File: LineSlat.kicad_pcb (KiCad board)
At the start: 4 copper layers, 100 x 160 mm, 130 parts, among them J4 DEBUG, J5 RJ45, J6 RJ45, J7 USB_B_Micro, J8 BATT, Q1 DMG3402, Q10 MMBT3904L, Q12 DMN6075S, Q13 MMBT3906, Q2 DMG3402, Q3 DMG3402, Q4 DMG3402, Q5 DMG3402, Q6 DMG3402, Q7 DMP3099L, Q8 MMBT3904L, Q9 DMN6075S, SW1 SPDT, SW2 SPDT, SW3 RESET, U1 THVD1400D, U2 THVD1400D, U3 RFM95W-915S2, U4 ATSAMD21G18A-A, U5 TSR1-2433E, Y1 32.768K-12.5p

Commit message: Change diodes and regulator
Changed regulator from TSR-1-2433E to TSR-1-2433
This changes Vin minimum from 6V to 4.76V

Changed schottky diodes to BAT54W.
This fixes 2 issues:
- reverse voltage 20V -> 30V (not enough margin for ~20V LiPo)
- forward voltage drop 600mV -> 250mV (5V-600mV is below Vin min of 3.3V regulator)
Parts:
- D3, D4: value SD103CW -> BAT54W
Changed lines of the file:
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@@
 			)
 		)
-		(property "Value" "SD103CW"
+		(property "Value" "BAT54W"
 			(at 0 2.1 90)
 			(layer "F.Fab")
@@
 			)
 		)
-		(property "Mouser Part Number" "78-SD103CW-HE3_A-08 "
+		(property "Mouser Part Number" "78-BAT54W-HG3-18 "
 			(at 0 0 90)
 			(unlocked yes)
@@
 			)
 		)
-		(property "Value" "SD103CW"
+		(property "Value" "BAT54W"
 			(at 0 2.1 90)
 			(layer "F.Fab")
@@
 			)
 		)
-		(property "Mouser Part Number" "78-SD103CW-HE3_A-08 "
+		(property "Mouser Part Number" "78-BAT54W-HG3-18 "
 			(at 0 0 -90)
 			(unlocked yes)

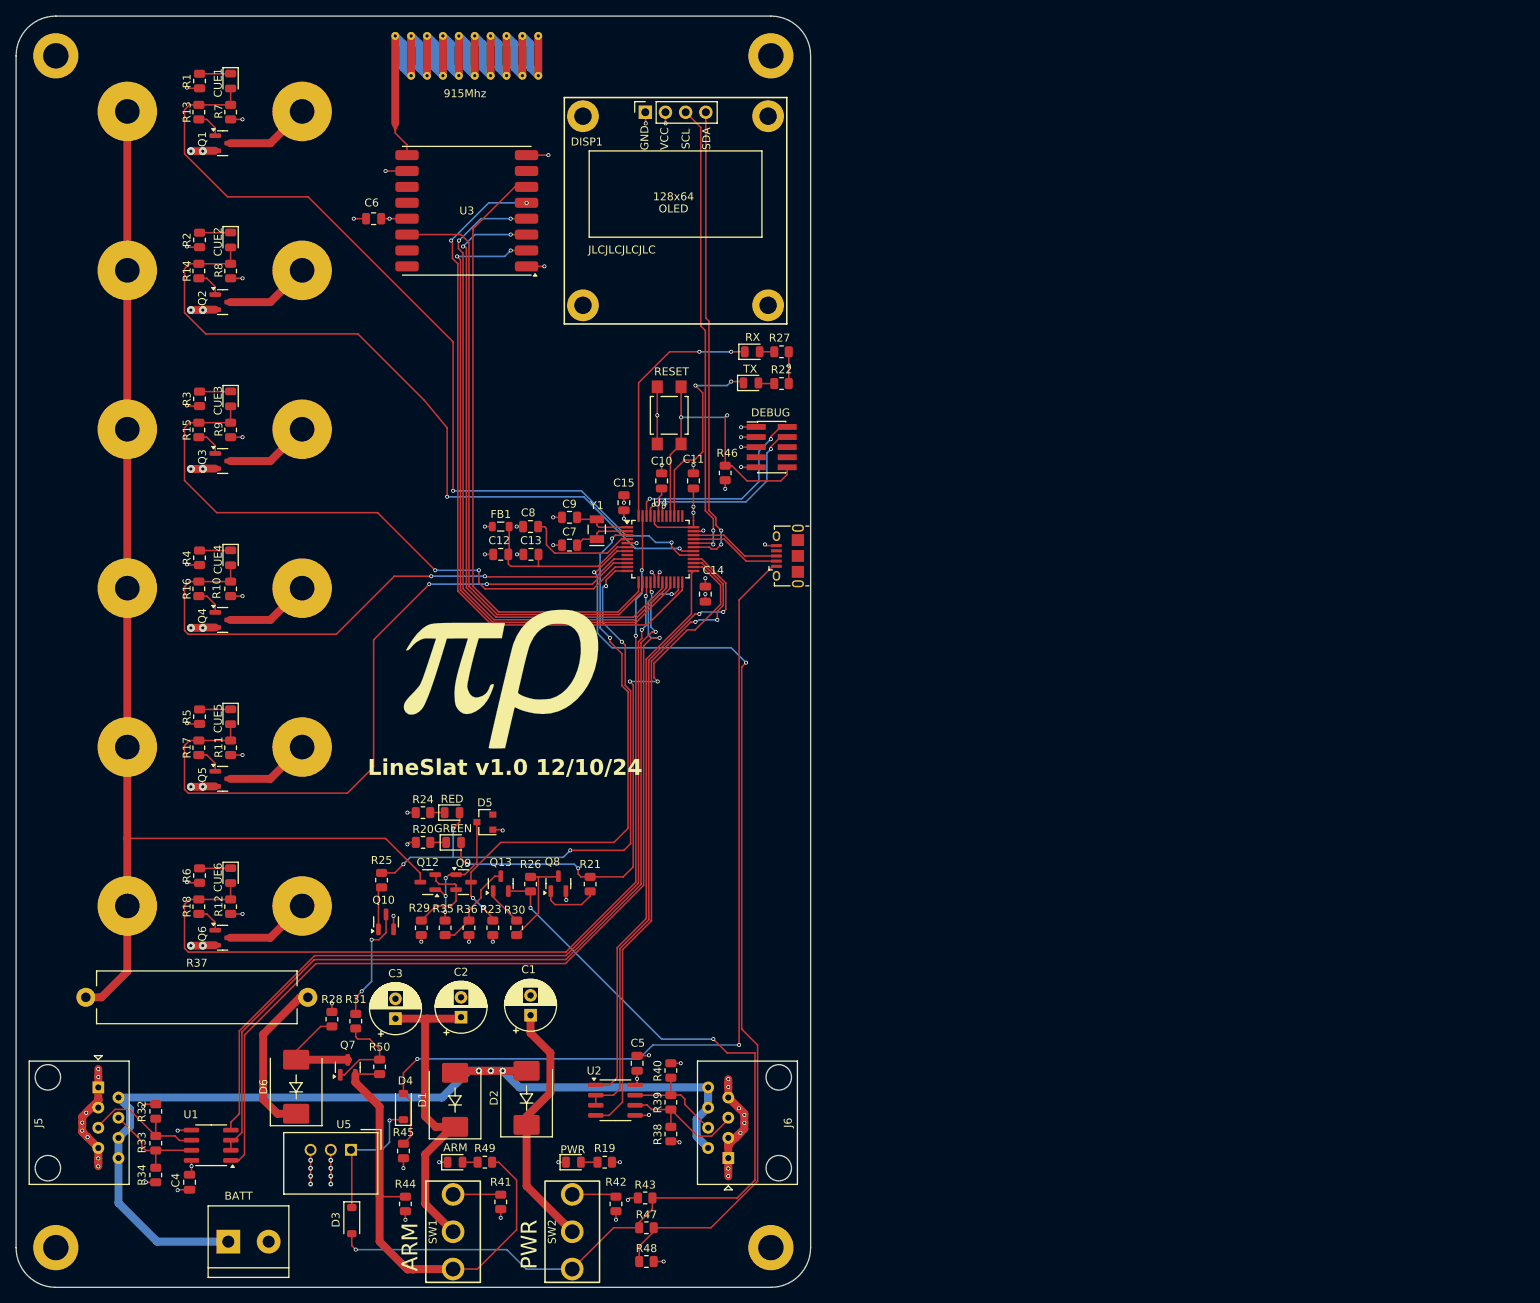
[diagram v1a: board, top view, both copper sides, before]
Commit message: v2.0
* new continuity test using INA219
* 8 cues instead of 6
* Lots of minor changes
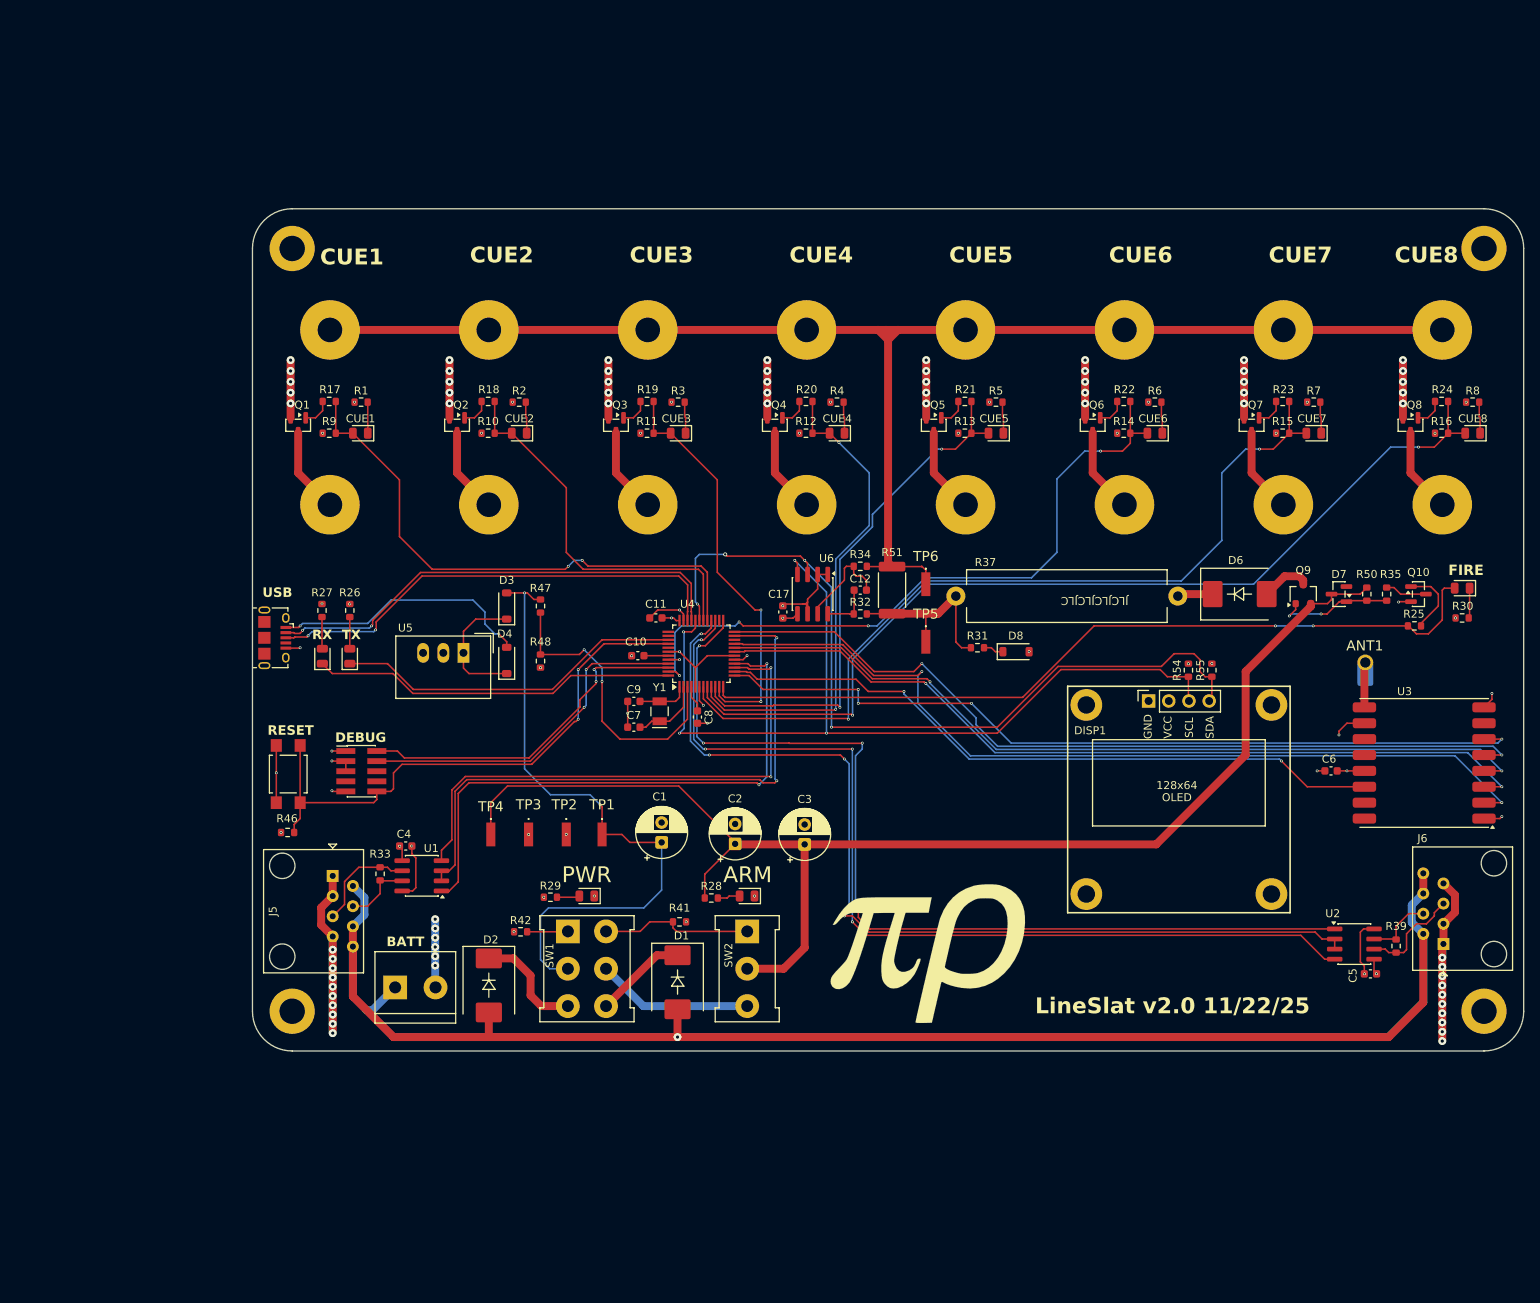
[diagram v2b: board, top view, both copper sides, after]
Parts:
- removed C13, C14, C15: 100n, Capacitor_SMD:C_0805_2012Metric
- removed D5: 15V, MyLib:D_SOT-23_ANK
- removed FB1: 1k5, Inductor_SMD:L_0805_2012Metric
- removed Q12: DMN6075S, Package_TO_SOT_SMD:SOT-23
- removed Q13: MMBT3906, Package_TO_SOT_SMD:SOT-23
- removed the Q9 at (86.3, 139.0)
- removed the R20 at (81.2, 134.0)
- removed the R21 at (102.2, 139.2)
- removed the R22 at (126.3, 76.2)
- removed the R28 at (69.8, 156.2)
- removed the R29 at (81.0, 144.8)
- removed the R30 at (93.0, 144.8)
- removed the R35 at (84.0, 144.8)
- removed R36: 10K, Resistor_SMD:R_0805_2012Metric
- removed R38, R40: 604R, Resistor_SMD:R_0805_2012Metric
- removed R43, R44: 1M, Resistor_SMD:R_0805_2012Metric
- removed R45: 100K, Resistor_SMD:R_0805_2012Metric
- added C17: 100n, Capacitor_SMD:C_0603_1608Metric, F.Cu at (126.5, 105.0)
- added CLIP15: PyroClip, MyLib:PyroClipRed, F.Cu at (189.5, 69.5)
- added CLIP16: PyroClip, MyLib:PyroClipRed, F.Cu at (209.5, 69.5)
- added CLIP7: PyroClip, MyLib:PyroClipBlack, F.Cu at (189.5, 91.5)
- added CLIP8: PyroClip, MyLib:PyroClipBlack, F.Cu at (209.5, 91.5)
- added D7: 10V, Package_TO_SOT_SMD:SOT-23, F.Cu at (196.5, 102.8)
- added D8: BAT54W, Diode_SMD:D_SOD-123, F.Cu at (155.8, 110.0)
- added LED7: RED, LED_SMD:LED_0805_2012Metric, F.Cu at (193.3, 82.5)
- added Q7: DMG3402, Package_TO_SOT_SMD:SOT-23, F.Cu at (185.5, 81.5)
- added R15: 1M, Resistor_SMD:R_0603_1608Metric, F.Cu at (189.4, 82.5)
- added R16: 1M, Resistor_SMD:R_0603_1608Metric, F.Cu at (209.4, 82.5)
- added R24: 100R, Resistor_SMD:R_0603_1608Metric, F.Cu at (209.4, 78.5)
- added R31: 150R, Resistor_SMD:R_0603_1608Metric, F.Cu at (151.0, 109.5)
- added R51: 100m 1% 3W, Resistor_SMD:R_2512_6332Metric, F.Cu at (140.2, 102.2)
- added R54: 10K, Resistor_SMD:R_0603_1608Metric, F.Cu at (177.6, 112.3)
- added R55: 10K, Resistor_SMD:R_0603_1608Metric, F.Cu at (180.5, 112.3)
- added R7: 1K, Resistor_SMD:R_0603_1608Metric, F.Cu at (193.3, 78.6)
- added R8: 1K, Resistor_SMD:R_0603_1608Metric, F.Cu at (213.3, 78.6)
- added TP1: RCTCTE, MyLib:RCTCTE, F.Cu at (103.8, 133.0)
- added TP2: RCTCTE, MyLib:RCTCTE, F.Cu at (99.2, 133.0)
- added TP3: RCTCTE, MyLib:RCTCTE, F.Cu at (94.5, 133.0)
- added TP4: RCTCTE, MyLib:RCTCTE, F.Cu at (89.8, 133.0)
- added TP5: RCTCTE, MyLib:RCTCTE, F.Cu at (144.5, 108.8)
- added TP6: RCTCTE, MyLib:RCTCTE, F.Cu at (144.5, 101.5)
- added U6: INA219B, Package_SO:SOIC-8_3.9x4.9mm_P1.27mm, F.Cu at (130.2, 102.8)
- ANT1: footprint RF_Antenna:Texas_SWRA416_868MHz_915MHz -> MyLib:Antenna915MHzSimpleCoil
- C10, C11, C4, C5, C6, C7, C8, C9: footprint Capacitor_SMD:C_0805_2012Metric -> Capacitor_SMD:C_0603_1608Metric
- C12: value 4u7 -> 100n; footprint Capacitor_SMD:C_0805_2012Metric -> Capacitor_SMD:C_0603_1608Metric
- H1, H2, H3, H4: value MountingHole -> MountingHole_3.2mm_M3_ISO7380_Pad
- LED8: value GREEN -> RED
- Q8: value MMBT3904L -> DMG3402
- Q9: renamed from Q7; value DMP3099L -> DMG3401; footprint Package_TO_SOT_SMD:SOT-23 -> MyLib:SC-59
- R1, R2, R25, R3, R4, R46, R47, R48, R5, R6: footprint Resistor_SMD:R_0805_2012Metric -> Resistor_SMD:R_0603_1608Metric
- R10: renamed from R8; value 10K -> 1M; footprint Resistor_SMD:R_0805_2012Metric -> Resistor_SMD:R_0603_1608Metric
- R11: renamed from R9; value 10K -> 1M; footprint Resistor_SMD:R_0805_2012Metric -> Resistor_SMD:R_0603_1608Metric
- R12: renamed from R10; value 10K -> 1M; footprint Resistor_SMD:R_0805_2012Metric -> Resistor_SMD:R_0603_1608Metric
- R13: renamed from R11; value 10K -> 1M; footprint Resistor_SMD:R_0805_2012Metric -> Resistor_SMD:R_0603_1608Metric
- R14: renamed from R12; value 10K -> 1M; footprint Resistor_SMD:R_0805_2012Metric -> Resistor_SMD:R_0603_1608Metric
- R17: renamed from R13; value 3K -> 100R; footprint Resistor_SMD:R_0805_2012Metric -> Resistor_SMD:R_0603_1608Metric
- R18: renamed from R14; value 3K -> 100R; footprint Resistor_SMD:R_0805_2012Metric -> Resistor_SMD:R_0603_1608Metric
- R19: renamed from R15; value 3K -> 100R; footprint Resistor_SMD:R_0805_2012Metric -> Resistor_SMD:R_0603_1608Metric
- R20: renamed from R16; value 3K -> 100R; footprint Resistor_SMD:R_0805_2012Metric -> Resistor_SMD:R_0603_1608Metric
- R21: renamed from R17; value 3K -> 100R; footprint Resistor_SMD:R_0805_2012Metric -> Resistor_SMD:R_0603_1608Metric
- R22: renamed from R18; value 3K -> 100R; footprint Resistor_SMD:R_0805_2012Metric -> Resistor_SMD:R_0603_1608Metric
- R23: value 100R 1% -> 100R; footprint Resistor_SMD:R_0805_2012Metric -> Resistor_SMD:R_0603_1608Metric
- R26: value 5K1 -> 510R; footprint Resistor_SMD:R_0805_2012Metric -> Resistor_SMD:R_0603_1608Metric
- R27: value 470R -> 510R; footprint Resistor_SMD:R_0805_2012Metric -> Resistor_SMD:R_0603_1608Metric
- R28: renamed from R49; footprint Resistor_SMD:R_0805_2012Metric -> Resistor_SMD:R_0603_1608Metric
- R29: renamed from R19; value 470R -> 510R; footprint Resistor_SMD:R_0805_2012Metric -> Resistor_SMD:R_0603_1608Metric
- R30: renamed from R24; footprint Resistor_SMD:R_0805_2012Metric -> Resistor_SMD:R_0603_1608Metric
- R32, R34: value 604R -> 10R; footprint Resistor_SMD:R_0805_2012Metric -> Resistor_SMD:R_0603_1608Metric
- R33, R39: value 110R -> 100R; footprint Resistor_SMD:R_0805_2012Metric -> Resistor_SMD:R_0603_1608Metric
- R35: renamed from R31; footprint Resistor_SMD:R_0805_2012Metric -> Resistor_SMD:R_0603_1608Metric
- R41: value 51K -> 5K1; footprint Resistor_SMD:R_0805_2012Metric -> Resistor_SMD:R_0603_1608Metric
- R42: value 51K -> 10K; footprint Resistor_SMD:R_0805_2012Metric -> Resistor_SMD:R_0603_1608Metric
- R50: value 20K -> 100K; footprint Resistor_SMD:R_0805_2012Metric -> Resistor_SMD:R_0603_1608Metric
- R9: renamed from R7; value 10K -> 1M; footprint Resistor_SMD:R_0805_2012Metric -> Resistor_SMD:R_0603_1608Metric
- SW1: value SPDT -> POWER; footprint MyLib:spdt_100SP1T1B2M2QE -> MyLib:DPDT-SW-T2-4E-B-A2-MA2
- SW2: value SPDT -> ARM; footprint MyLib:spdt_100SP1T1B2M2QE -> MyLib:SPDT-SW-T2-2E-A-A2-M1
- U5: value TSR1-2433E -> TSR1-2433; footprint Converter_DCDC:Converter_DCDC_TRACO_TSR1-xxxxE_THT -> Converter_DCDC:Converter_DCDC_TRACO_TSR-1_THT
- moved H3 182.2 mm to (214.8, 155.2)
- moved H1 181.4 mm to (214.8, 59.2)
- moved R35 140.4 mm to (202.5, 102.8)
- moved H4 139.4 mm to (64.8, 59.2)
- moved C6 139.1 mm to (195.5, 125.0)
- moved U3 139.1 mm to (207.2, 124.0)
- moved LED8 138.2 mm to (213.3, 82.5), turned to 180 degrees
- moved R50 137.8 mm to (200.0, 102.8), turned to 90 degrees
- moved Q10 136.3 mm to (206.5, 102.8), turned to 0 degrees
- moved ANT1 134.6 mm to (199.8, 111.4), turned to 90 degrees
- moved H2 134.5 mm to (64.8, 155.2)
- moved Q9 134.2 mm to (192.0, 102.8)
- moved R6 134.2 mm to (173.3, 78.6), turned to 0 degrees
- moved D6 134.0 mm to (184.0, 102.8), turned to 0 degrees
- moved R25 133.9 mm to (206.0, 106.8), turned to 0 degrees
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- renumbered CLIP11 to CLIP10, CLIP10 to CLIP11, CLIP9 to CLIP12, CLIP8 to CLIP13, CLIP7 to CLIP14, CLIP12 to CLIP9, LED9 to LED10, LED7 to LED13, LED10 to LED9
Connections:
- net /COMM_A2 renamed /COM2+
- net /COMM_B2 renamed /COM2-
- net /D9_FIRE_ENA renamed /D9_FIRE
- net /VDDCORE renamed Net-(U4-VDDCORE)
- C1 pad 1: Net-(D2-K) -> +18V
- C12 pad 1: /VDDANA -> Net-(U6-IN+)
- C12 pad 2: GND -> Net-(U6-IN-)
- C2 pad 1: Net-(D1-K) -> V_ARM
- C3 pad 1: Net-(D1-K) -> V_ARM
- H1 pad 1: GND -> (no net)
- H2 pad 1: GND -> (no net)
- H3 pad 1: GND -> (no net)
- H4 pad 1: GND -> (no net)
- J5 pad 4: /COMM_B1 -> /COM1-
- J5 pad 5: /COMM_A1 -> /COM1+
- LED10 pad 2: Net-(LED9-A) -> Net-(LED10-A)
- LED8 pad 2: /D13_CONT_CHECK -> /A2_CUE8
- Q8 pad 3: Net-(Q8-C) -> /L8
- Q9 pad 2: /V_ARM -> V_ARM
- R23 pad 1: /A0_CONT_SENSE -> /A1_CUE7
- R23 pad 2: +3V3 -> Net-(Q7-G)
- R26 pad 1: Net-(Q8-C) -> +3V3
- R26 pad 2: +18V -> Net-(LED10-A)
- R28 pad 1: /V_ARM -> V_ARM
- R32 pad 1: +3V3 -> Net-(R31-Pad2)
- R32 pad 2: /COMM_A1 -> Net-(U6-IN+)
- R33 pad 1: /COMM_A1 -> /COM1+
- R33 pad 2: /COMM_B1 -> /COM1-
- R34 pad 1: /COMM_B1 -> /ECOMMON
- R34 pad 2: GND -> Net-(U6-IN-)
- R37 pad 1: /ECOMMON -> Net-(R31-Pad2)
- R41 pad 2: Net-(SW1-C) -> Net-(SW1B-A)
- R42 pad 2: Net-(SW2-C) -> Net-(SW1A-A)
- R47 pad 2: /A1_BAT_SENSE -> /A0_VBAT
- R48 pad 1: /A1_BAT_SENSE -> /A0_VBAT
- R50 pad 2: /V_ARM -> V_ARM
- SW1 pad 1: /V_ARM -> Net-(SW1A-A)
- SW1 pad 2: Net-(D1-K) -> +18V
- SW1 pad 3: Net-(SW1-C) -> Net-(D2-K)
- SW2 pad 1: +18V -> Net-(SW1B-A)
- SW2 pad 2: Net-(D2-K) -> V_ARM
- SW2 pad 3: Net-(SW2-C) -> Net-(SW1B-B)
- U1 pad 6: /COMM_A1 -> /COM1+
- U1 pad 7: /COMM_B1 -> /COM1-
- U4 pad 26: /D13_CONT_CHECK -> /D13
- U4 pad 3: /A0_CONT_SENSE -> /A0_VBAT
- U4 pad 6: /VDDANA -> +3V3
- U4 pad 7: /A1_BAT_SENSE -> /A1_CUE7
- U4 pad 8: /A2 -> /A2_CUE8
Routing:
- net +BAT: track 125.9 -> 336.1 mm, vias 3 -> 1
- net V_ARM: track 0.00 -> 167.9 mm
- net /A2_CUE8: track 0.00 -> 120.5 mm, vias 0 -> 2
- net /A1_BAT_SENSE: track 119.7 -> 0.00 mm, vias 2 -> 0
- net /A1_CUE7: track 0.00 -> 106.8 mm, vias 0 -> 2
- net /VBUS: track 115.4 -> 33.0 mm
- net /D13_CONT_CHECK: track 73.3 -> 0.00 mm, vias 4 -> 0
- net /A0_CONT_SENSE: track 69.6 -> 0.00 mm, vias 4 -> 0
- net /V_ARM: track 59.6 -> 0.00 mm
- net /SCL: track 58.4 -> 111.7 mm, vias 2 -> 4
- net /D11_RX2: track 70.8 -> 120.6 mm, vias 0 -> 4
- net /USB_D-: track 11.6 -> 59.9 mm, vias 0 -> 2
- net /USB_D+: track 11.5 -> 59.3 mm, vias 0 -> 2
- net /D7_CUE2: track 95.4 -> 48.2 mm, vias 2 -> 0
- net GND: track 140.1 -> 184.8 mm, vias 89 -> 106
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- added copper zone on In1.Cu, net +3V3
- added copper zone on In2.Cu, net GND
- removed copper zone on In2.Cu, net +3V3
- removed copper zone on In1.Cu, net GND
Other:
- board size 100 x 160 mm -> 160 x 106 mm
- board text added: "CUE7"
- board text added: "CUE8"
- board text added: "FIRE"
- board text added: "LineSlat v2.0 11/22/25"
- board text added: "USB"
- board text removed: "LineSlat v1.0 12/10/24"

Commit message: Added files for 3d printed boxes using openscad
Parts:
- R29: value 510R -> 2K
